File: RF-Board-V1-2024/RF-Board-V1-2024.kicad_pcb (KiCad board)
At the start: 2 copper layers, 100 x 100 mm, 129 parts, among them J2 RFPC-SMA29-F, J3 RFPC-SMA29-F, J4 UART, J5 RFPC-SMA28-F, J6 RFPC-SMA29-F, J8 USB_C_Receptacle_USB2.0_14P, J9 MSD-10-C, SW1 SW_SPST, SW2 SW_SPST, SW3 SW_SPST, SW4 SW_SPST, SW5 SW_SPST, SW6 SW_SPST, SW7 SW_DPDT_x2, U1 AZ1084-3.3, U3 TPS2596, U4 AZ1084-5.0, U5 MCP2542FD, U6 STM32G484RET6, U7 USBLC6-2SC6, X1 OXETDLJANF-8MHZ

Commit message: idk what this is
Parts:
- SW1, SW2: footprint Button_Switch_SMD:SW_DIP_SPSTx01_Slide_6.7x4.1mm_W6.73mm_P2.54mm_LowProfile_JPin -> Button_Switch_THT:SW_PUSH_6mm
- moved SW7 10.9 mm to (76.0, 65.5), turned to -90 degrees
- moved C36 10.0 mm to (96.9, 63.1)
- moved C37 10.0 mm to (96.9, 69.2)
- moved SW1 6.93 mm to (86.5, 60.9)
- moved SW2 6.55 mm to (86.5, 69.3)
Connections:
- net /868.MISO renamed /24.MISO
- net /868.MOSI renamed /24.MOSI
- net /868.SCK renamed /24.SCK

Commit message: routed
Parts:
- added D16: LED, LED_SMD:LED_0805_2012Metric, F.Cu at (134.5, 76.5)
- added R30: 600, Resistor_SMD:R_0805_2012Metric, F.Cu at (134.5, 74.5)
- C13, C5, R19, R5, U5: moved to B.Cu
- H1, H2, H3, H4: value MountingHole -> ~
- moved C4 57.4 mm to (82.8, 65.0), turned to 180 degrees
- moved C2 55.6 mm to (87.4, 69.6), turned to 0 degrees
- moved D3 52.6 mm to (76.5, 78.7)
- moved R10 52.6 mm to (76.5, 74.8)
- moved U1 49.3 mm to (82.8, 75.7), turned to 90 degrees
- moved SW2 44.2 mm to (122.2, 95.5), turned to 90 degrees
- moved SW1 44.0 mm to (113.7, 95.5), turned to 90 degrees
- moved SW7 37.0 mm to (109.3, 81.7)
- moved D11 36.2 mm to (92.8, 64.4)
- moved R20 36.1 mm to (96.7, 64.4)
- moved C1 35.7 mm to (88.3, 81.8)
- moved R19 35.3 mm to (115.0, 110.3), turned to 0 degrees
- moved C37 32.2 mm to (124.2, 86.3), turned to 180 degrees
- moved R5 31.7 mm to (109.1, 114.2), turned to -90 degrees
- moved U5 31.3 mm to (114.0, 114.2)
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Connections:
- J9 pad 05: /SD/SD.SCLK -> /SD.SCLK
- U6 pad 18: /24.SCK -> /GPIO_SWT2
- U6 pad 19: /24.MOSI -> /24.SCK
- U6 pad 20: /24.MISO -> /24.MOSI
- U6 pad 21: /GPIO_SWT2 -> /24.MISO
- U6 pad 33: /CAN_STBY -> /GPIO_LED6
- U6 pad 38: /24.DIO3 -> /24.BUSY
- U6 pad 39: /24.DIO2 -> /24.DIO1
- U6 pad 40: /24.DIO1 -> /24.DIO2
- U6 pad 41: /24.BUSY -> /24.DIO3
- U6 pad 50: /868.DIO0 -> /868.DIO5
- U6 pad 51: /868.DIO1 -> /868.DIO3
- U6 pad 52: /868.DIO2 -> /868.DIO4
- U6 pad 53: /868.DIO3 -> /868.DIO0
- U6 pad 54: /868.DIO4 -> /868.DIO1
- U6 pad 55: /868.DIO5 -> /868.DIO2
- U6 pad 57: /915.DIO0 -> /915.DIO5
- U6 pad 58: /915.DIO1 -> /915.DIO3
- U6 pad 59: /915.DIO2 -> /915.DIO4
- U6 pad 6: /SD.SCLCK -> /SD.SCLK
- U6 pad 60: /915.DIO3 -> /915.DIO0
- U6 pad 61: /915.DIO4 -> /915.DIO1
- U6 pad 62: /915.DIO5 -> /915.DIO2
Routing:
- net +3.3V: track 0.00 -> 533.6 mm, vias 0 -> 31
- net GND: track 0.00 -> 156.3 mm, vias 0 -> 81
- net +5V: track 0.00 -> 88.9 mm, vias 0 -> 3
- net /24.SCK: track 0.00 -> 86.2 mm, vias 0 -> 2
- net /SD.NSS: track 0.00 -> 84.2 mm, vias 0 -> 2
- net /24.NSS: track 0.00 -> 81.2 mm, vias 0 -> 4
- net /24.MOSI: track 0.00 -> 80.9 mm, vias 0 -> 2
- net /SD.SCLK: track 0.00 -> 79.6 mm, vias 0 -> 2
- net /24.MISO: track 0.00 -> 78.3 mm, vias 0 -> 2
- net /24.RST: track 0.00 -> 75.3 mm, vias 0 -> 2
- net /915.NSS: track 0.00 -> 71.3 mm, vias 0 -> 2
- net /24.RXEN: track 0.00 -> 70.2 mm, vias 0 -> 2
- net /915.RST: track 0.00 -> 69.7 mm, vias 0 -> 2
- net /24.TXEN: track 0.00 -> 69.1 mm, vias 0 -> 2
- net /~{GNSS.RST}: track 0.00 -> 63.5 mm, vias 0 -> 4
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- added copper zone on B.Cu, net GND
- added copper zone on F.Cu, net GND

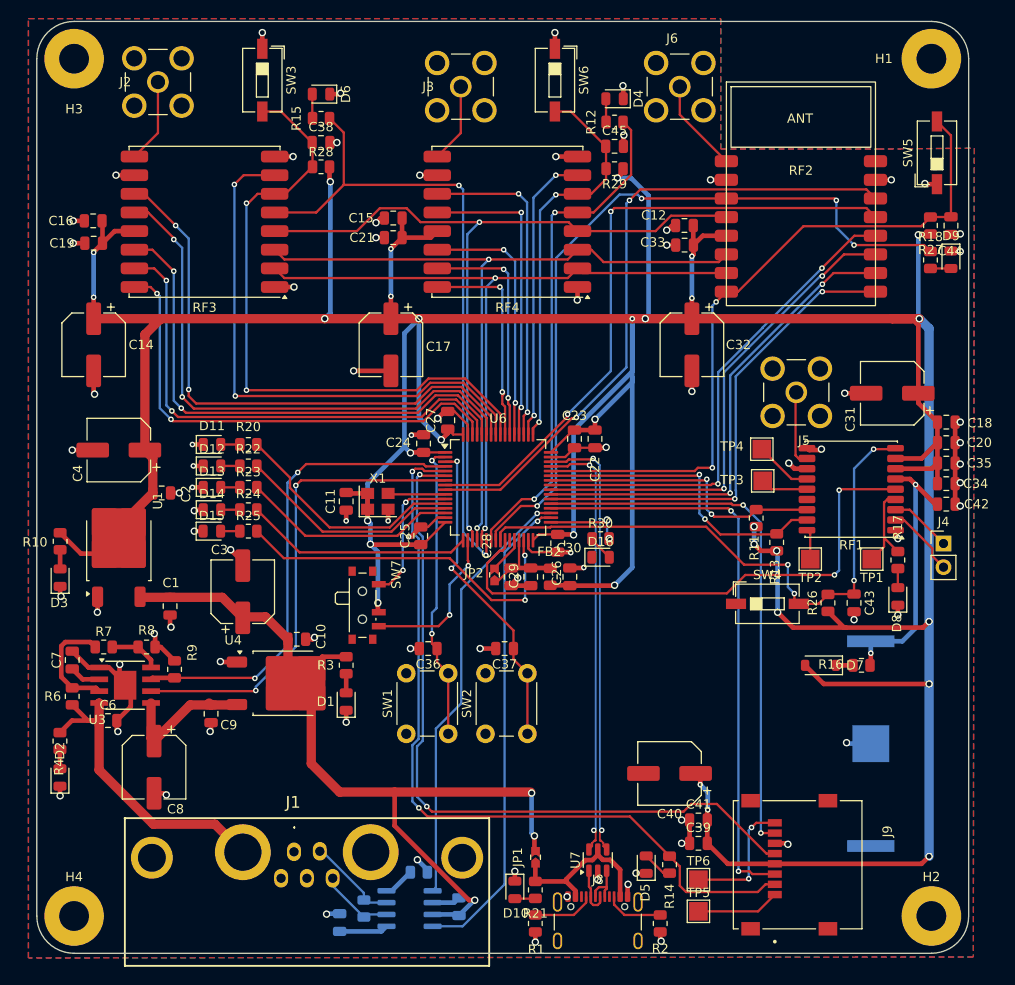
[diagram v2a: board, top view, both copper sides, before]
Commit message: cyhanged buttons
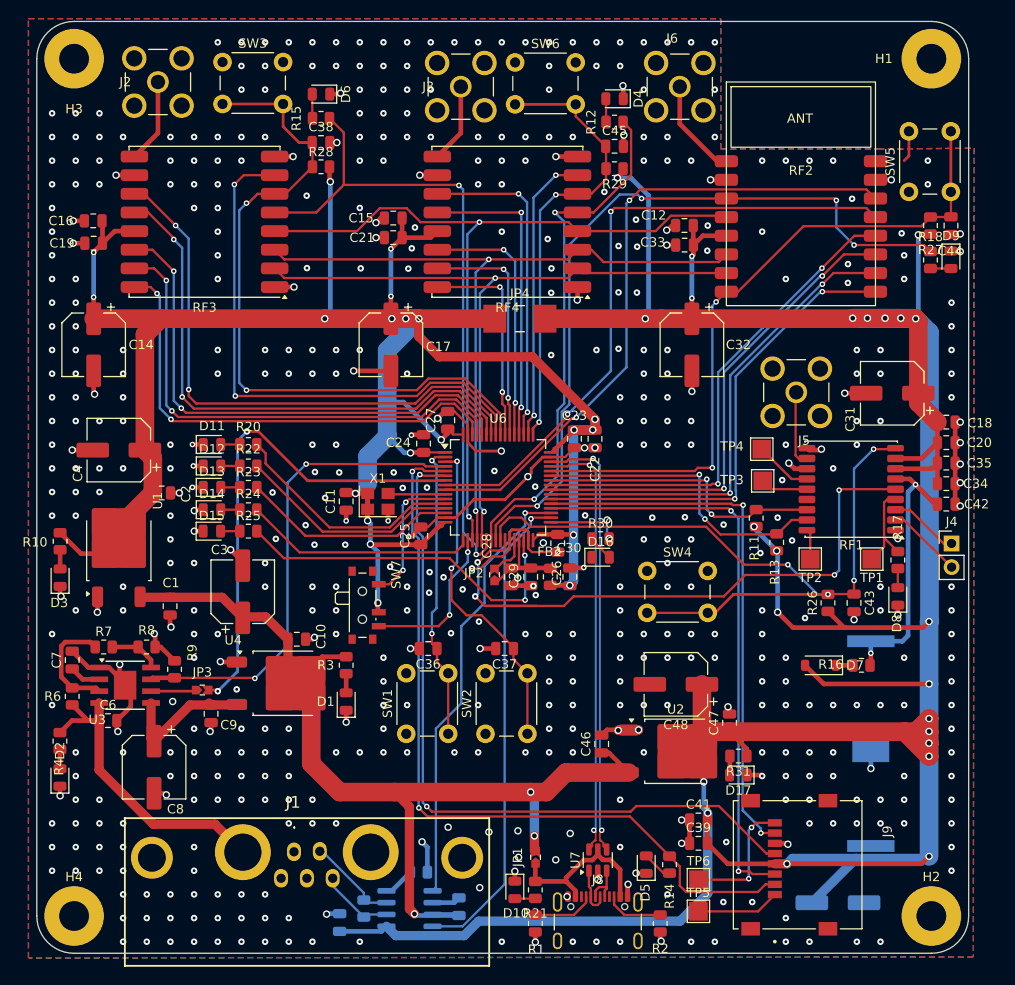
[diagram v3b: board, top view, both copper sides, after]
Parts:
- added C46: 10u, Capacitor_SMD:C_0805_2012Metric, F.Cu at (134.6, 96.5)
- added C47: 22u, Capacitor_SMD:C_0805_2012Metric, F.Cu at (148.3, 94.3)
- added C48: 100u, Capacitor_SMD:CP_Elec_6.3x5.9, F.Cu at (142.6, 90.1)
- added D17: LED, LED_SMD:LED_0805_2012Metric, F.Cu at (149.3, 99.9)
- added JP3: Jumper_2_Open, ecocad_lib_footprints:J_0603_Triangular, F.Cu at (91.8, 90.7)
- added JP4: Jumper_2_Open, digikey-footprints:Jumper_Micro-Miniature_P5.375mm, F.Cu at (125.8, 50.9)
- added R31: 600, Resistor_SMD:R_0805_2012Metric, F.Cu at (149.3, 97.8)
- added U2: AZ1084-3.3, Package_TO_SOT_SMD:TO-252-2, F.Cu at (142.6, 97.3)
- C40: moved to B.Cu
- SW3, SW4, SW5, SW6: footprint Button_Switch_SMD:SW_DIP_SPSTx01_Slide_6.7x4.1mm_W6.73mm_P2.54mm_LowProfile_JPin -> Button_Switch_THT:SW_PUSH_6mm
- moved C40 22.8 mm to (160.0, 113.6), turned to 0 degrees
- moved SW4 13.4 mm to (139.5, 78.0)
- moved SW5 5.16 mm to (167.6, 37.3)
- moved SW3 4.69 mm to (93.9, 23.4), turned to 0 degrees
- moved SW6 4.67 mm to (125.3, 23.4), turned to 0 degrees
- moved J4 0.87 mm to (172.2, 75.0)
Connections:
- net /24.MISO renamed /868.MISO
- net /24.MOSI renamed /868.MOSI
- net /24.SCK renamed /868.SCK
- J8 pad S1: GND -> unconnected-(J8-SHIELD-PadS1)_1
- U6 pad 7: /~{FAULT} -> Net-(JP3-B)
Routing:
- net +3.3V: track 533.6 -> 675.6 mm, vias 31 -> 43
- net Net-(JP3-B): track 0.00 -> 53.9 mm, vias 0 -> 2
- net /~{FAULT}: track 51.3 -> 4.71 mm, vias 2 -> 0
- net GND: track 156.3 -> 191.0 mm, vias 81 -> 540
- net /~{GNSS.RST}: track 63.5 -> 82.3 mm
- net +5V: track 88.9 -> 106.7 mm
- net /GNSS.EXTINT: track 59.8 -> 69.6 mm, vias 2 -> 4
- net /915.RST: track 69.7 -> 76.3 mm
- net /868.RST: track 43.4 -> 48.7 mm
- net Net-(D17-A): track 0.00 -> 2.05 mm
- net /24.RST: track 75.3 -> 73.6 mm
- net /868.NSS: track 54.7 -> 55.9 mm
- net /GPIO_BTN2: track 34.2 -> 35.1 mm
- net Net-(J4-Pin_1): track 6.65 -> 7.52 mm
- net /CAN_TX: track 46.6 -> 47.4 mm
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
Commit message: A
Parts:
- moved C8 3.07 mm to (89.7, 98.9), turned to 0 degrees
- moved H3 1.66 mm to (79.0, 24.3)
- moved H1 1.62 mm to (169.0, 24.3)
- moved J1 1.43 mm to (103.0, 108.3)
- moved H4 1.24 mm to (79.0, 114.3)
- moved H2 1.20 mm to (169.0, 114.3)
- moved D10 0.96 mm to (125.2, 111.2)
- moved JP1 0.96 mm to (127.4, 107.7)
- moved R21 0.96 mm to (127.4, 111.2)
- moved U7 0.96 mm to (134.1, 108.0)
- moved D5 0.96 mm to (139.3, 108.5)
- moved R14 0.96 mm to (141.8, 108.5)
- moved R2 0.96 mm to (140.8, 114.8)
- moved R1 0.96 mm to (127.4, 114.8)
- moved J8 0.96 mm to (134.1, 115.6)
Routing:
- net GND: track 191.0 -> 201.5 mm, vias 540 -> 529
- net /GNSS.EXTINT: track 69.6 -> 64.0 mm
- net /Power_CAN/FUSE_OUT: track 15.0 -> 20.3 mm
- net /SD.NSS: track 83.6 -> 86.5 mm
- net +5V: track 106.7 -> 104.6 mm
- net /Power_CAN/VBUS: track 18.5 -> 20.4 mm
- net /Power_CAN/CAN_L: track 8.09 -> 9.49 mm
- net /Power_CAN/CAN_H: track 9.88 -> 11.3 mm
- net /USB_D+: track 47.5 -> 46.5 mm
- net /USB_D-: track 46.4 -> 45.5 mm
- net /SD.SCLK: track 78.9 -> 79.6 mm
- net /Power_CAN/7V_UnProtected: track 34.6 -> 34.1 mm
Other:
- outline, holes or cut-outs redrawn

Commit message: A
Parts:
- added G***: LOGO, LOGO, F.Cu at (156.5, 22.0)
- added G***: LOGO, LOGO, F.Cu at (129.8, 57.1)
- added G***: LOGO, ecocad_lib_footprints:FacEngg Tag, B.Cu at (109.4, 39.2)
- added kibuzzard-6785DED4: G***, kibuzzard-6785DED4, F.Cu at (141.7, 60.1)
- added kibuzzard-6785DF01: G***, kibuzzard-6785DF01, F.Cu at (139.3, 61.4)
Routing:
- net +3.3V: track 675.6 -> 683.0 mm, vias 43 -> 46
- net GND: vias 529 -> 530

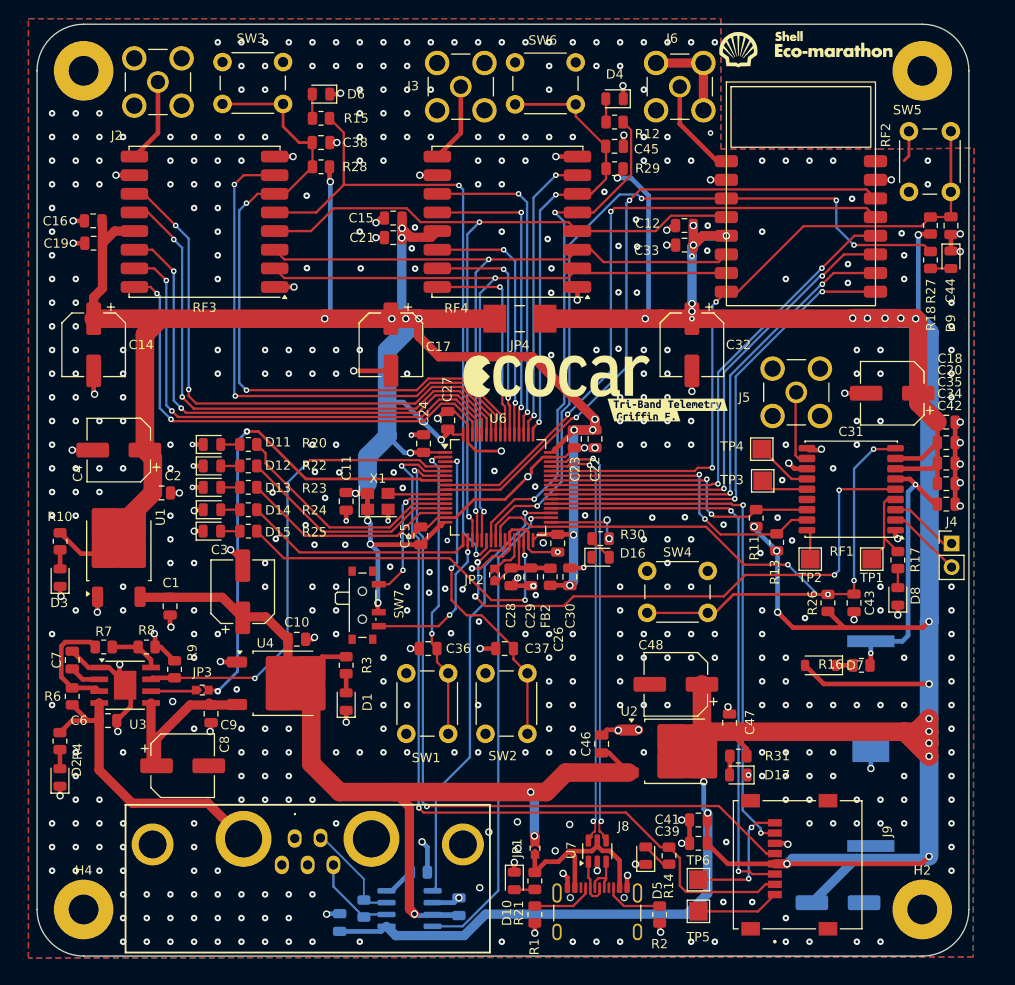
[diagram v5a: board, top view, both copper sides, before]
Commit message: need to reroute this
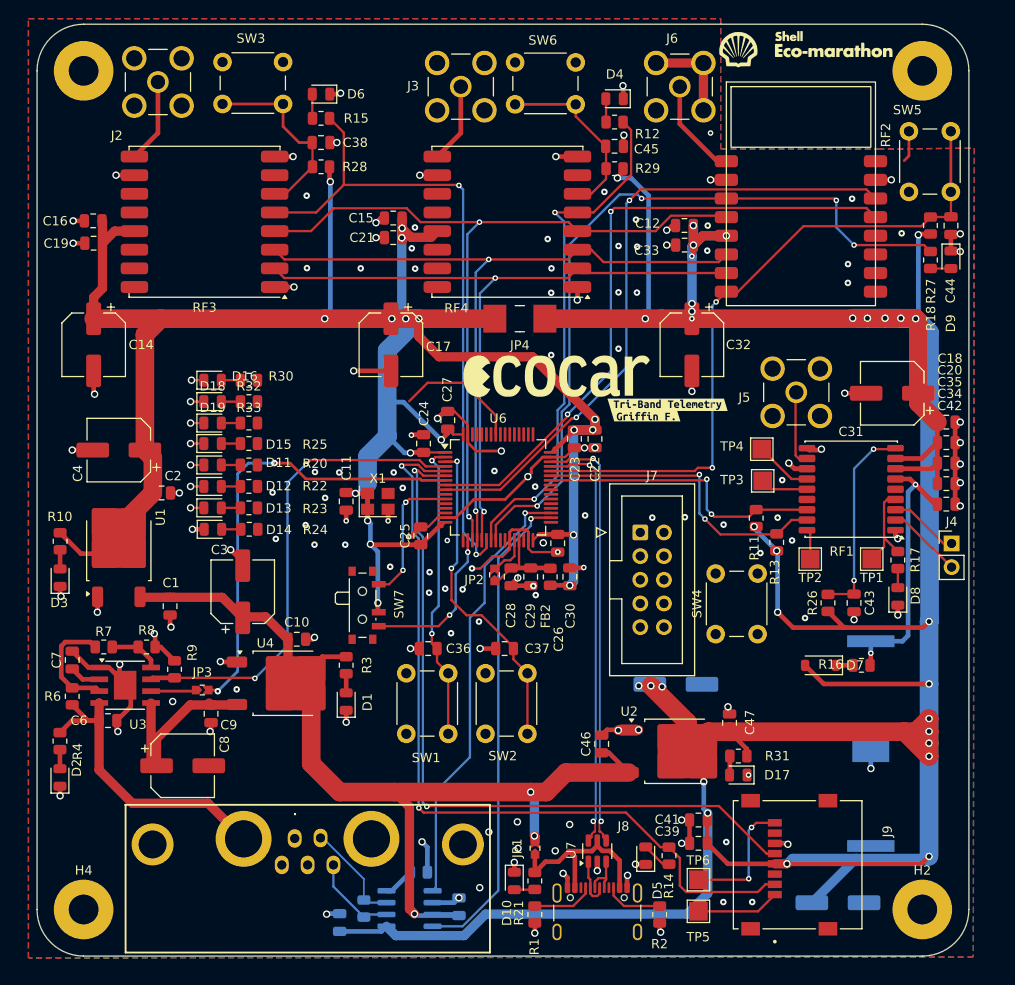
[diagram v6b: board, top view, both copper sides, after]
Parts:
- added D18: LED, LED_SMD:LED_0805_2012Metric, F.Cu at (92.9, 59.8)
- added D19: LED, LED_SMD:LED_0805_2012Metric, F.Cu at (92.9, 62.1)
- added J7: STM32-Prog-Header, ecocad_lib_footprints:IDC-STM32-Prog-Header_2x05_P2.54mm_Vertical, F.Cu at (138.8, 73.8)
- added R32: 1k, Resistor_SMD:R_0805_2012Metric, F.Cu at (96.8, 59.8)
- added R33: 1k, Resistor_SMD:R_0805_2012Metric, F.Cu at (96.8, 62.1)
- C48: moved to B.Cu
- R20, R22, R23, R24, R25, R30: value 600 -> 1k
- R27, R28: value 10k -> 0R
- R29: value 0 -> 0R
- moved D16 45.8 mm to (92.9, 57.5)
- moved R30 41.4 mm to (96.8, 57.5)
- moved SW4 10.00 mm to (146.8, 84.8), turned to 90 degrees
- moved D15 9.40 mm to (92.9, 64.3)
- moved R25 9.40 mm to (96.8, 64.3)
- moved D12 2.20 mm to (92.9, 68.9)
- moved D13 2.20 mm to (92.9, 71.2)
- moved R22 2.20 mm to (96.8, 68.9)
- moved R23 2.20 mm to (96.8, 71.2)
- moved D11 2.20 mm to (92.9, 66.6)
- moved R20 2.20 mm to (96.8, 66.6)
- moved D14 2.10 mm to (92.9, 73.5)
- moved R24 2.10 mm to (96.8, 73.5)
- moved G*** 0.47 mm to (109.5, 39.6)
- turned C48 to 0 degrees
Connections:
- net /868.MISO renamed /24.MISO
- net /868.MOSI renamed /24.MOSI
- net /868.SCK renamed /24.SCK
- U6 pad 10: /XCLK -> /SD.NSS
- U6 pad 30: /GPIO_LED5 -> /915.DIO0
- U6 pad 33: /GPIO_LED6 -> /CAN_STBY
- U6 pad 36: /SD.MOSI -> /SD.MISO
- U6 pad 37: /SD.MISO -> /SD.MOSI
- U6 pad 38: /24.BUSY -> /24.DIO3
- U6 pad 39: /24.DIO1 -> /24.DIO2
- U6 pad 40: /24.DIO2 -> /24.DIO1
- U6 pad 41: /24.DIO3 -> /24.BUSY
- U6 pad 49: /868.RST -> /SW_CLK
- U6 pad 5: /SD.NSS -> /XCLK
- U6 pad 50: /868.DIO5 -> /SW_DIO
- U6 pad 51: /868.DIO3 -> unconnected-(U6-PA15-Pad51)
- U6 pad 52: /868.DIO4 -> /868.RST
- U6 pad 54: /868.DIO1 -> /868.DIO4
- U6 pad 55: /868.DIO2 -> /868.DIO5
- U6 pad 58: /915.DIO3 -> /915.DIO4
- U6 pad 59: /915.DIO4 -> /GPIO_LED5
- U6 pad 60: /915.DIO0 -> /GPIO_LED6
- U6 pad 61: /915.DIO1 -> /GPIO_LED7
- U6 pad 62: /915.DIO2 -> /GPIO_LED8
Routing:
- net /GNSS.EXTINT: track 64.0 -> 0.00 mm, vias 4 -> 0
- net /SD.MOSI: track 62.5 -> 0.00 mm, vias 2 -> 0
- net /915.DIO3: track 61.5 -> 0.00 mm, vias 2 -> 0
- net /~{GNSS.RST}: track 82.3 -> 21.6 mm, vias 4 -> 2
- net /915.DIO4: track 59.7 -> 0.00 mm, vias 2 -> 0
- net /SD.MISO: track 58.2 -> 0.00 mm, vias 2 -> 0
- net /915.DIO0: track 56.1 -> 0.00 mm, vias 2 -> 0
- net /915.RST: track 76.3 -> 20.6 mm, vias 2 -> 0
- net /915.DIO1: track 54.4 -> 0.00 mm, vias 2 -> 0
- net /24.DIO3: track 52.9 -> 0.00 mm, vias 2 -> 0
- net /24.DIO2: track 52.6 -> 0.00 mm, vias 2 -> 0
- net /915.DIO2: track 52.2 -> 0.00 mm, vias 2 -> 0
- net /24.DIO1: track 52.1 -> 0.00 mm, vias 2 -> 0
- net /24.BUSY: track 51.7 -> 0.00 mm, vias 2 -> 0
- net /915.DIO5: track 59.5 -> 13.6 mm, vias 2 -> 0
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
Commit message: done?
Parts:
- moved R24 11.1 mm to (96.5, 62.4)
- moved R22 11.1 mm to (96.5, 57.8)
- moved R23 11.1 mm to (96.5, 60.1)
- moved R20 11.1 mm to (96.5, 55.5)
- moved D14 11.1 mm to (92.7, 62.4)
- moved D12 11.1 mm to (92.7, 57.8)
- moved D13 11.1 mm to (92.7, 60.1)
- moved D11 11.1 mm to (92.7, 55.5)
- moved R30 9.50 mm to (96.5, 67.0)
- moved R32 9.50 mm to (96.5, 69.3)
- moved R33 9.50 mm to (96.5, 71.6)
- moved D16 9.50 mm to (92.7, 67.0)
- moved D18 9.50 mm to (92.7, 69.3)
- moved D19 9.50 mm to (92.7, 71.6)
- moved C11 2.45 mm to (107.3, 68.0)
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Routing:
- net /915.DIO0: track 0.00 -> 73.9 mm, vias 0 -> 6
- net /SD.MOSI: track 0.00 -> 65.9 mm, vias 0 -> 2
- net /915.DIO4: track 0.00 -> 63.8 mm, vias 0 -> 4
- net /24.DIO3: track 0.00 -> 61.1 mm, vias 0 -> 2
- net /SD.MISO: track 0.00 -> 59.6 mm, vias 0 -> 2
- net /24.DIO2: track 0.00 -> 59.2 mm, vias 0 -> 2
- net /GNSS.EXTINT: track 0.00 -> 58.3 mm, vias 0 -> 4
- net /24.DIO1: track 0.00 -> 56.3 mm, vias 0 -> 4
- net /~{GNSS.RST}: track 21.6 -> 76.9 mm, vias 2 -> 4
- net /24.BUSY: track 0.00 -> 53.9 mm, vias 0 -> 4
- net /915.RST: track 20.6 -> 71.6 mm, vias 0 -> 2
- net /SW_DIO: track 0.00 -> 41.5 mm, vias 0 -> 2
- net /915.DIO5: track 13.6 -> 54.5 mm, vias 0 -> 2
- net /GPIO_LED1: track 0.00 -> 36.9 mm, vias 0 -> 2
- net /868.DIO5: track 0.00 -> 35.7 mm, vias 0 -> 2
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
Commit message: Helped Griff with some traces and optimizing routing
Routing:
- net GND: track 211.5 -> 186.6 mm, vias 152 -> 150
- net /GPIO_LED2: track 22.0 -> 34.2 mm
- net +3.3V: track 709.7 -> 702.8 mm, vias 50 -> 49
- net Net-(JP3-B): track 45.1 -> 43.5 mm, vias 4 -> 2
- net /SD.NSS: track 79.1 -> 77.9 mm, vias 5 -> 4
- net /915.RST: track 71.6 -> 72.8 mm
- net /GPIO_LED1: track 36.9 -> 38.0 mm
- net Net-(JP2-B): track 5.17 -> 4.12 mm
- net /GPIO_LED8: track 31.6 -> 30.5 mm
- net /24.RST: track 79.5 -> 80.4 mm
- net /GPIO_LED3: track 30.2 -> 30.9 mm
- net /24.BUSY: track 53.9 -> 54.6 mm
- net /SW_CLK: track 33.2 -> 32.6 mm
